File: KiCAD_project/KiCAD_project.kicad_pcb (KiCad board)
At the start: 2 copper layers, 3.6 x 3.3 mm, 17 parts, among them J1 Conn_01x04_Pin, SW1 SW_Push, SW10 RotaryEncoder_Switch, SW2 SW_Push, SW3 SW_Push, SW4 SW_Push, SW5 SW_Push, SW6 SW_Push, SW7 SW_Push, SW8 SW_Push, SW9 SW_Push, U1 XIAO-RP2040-DIP

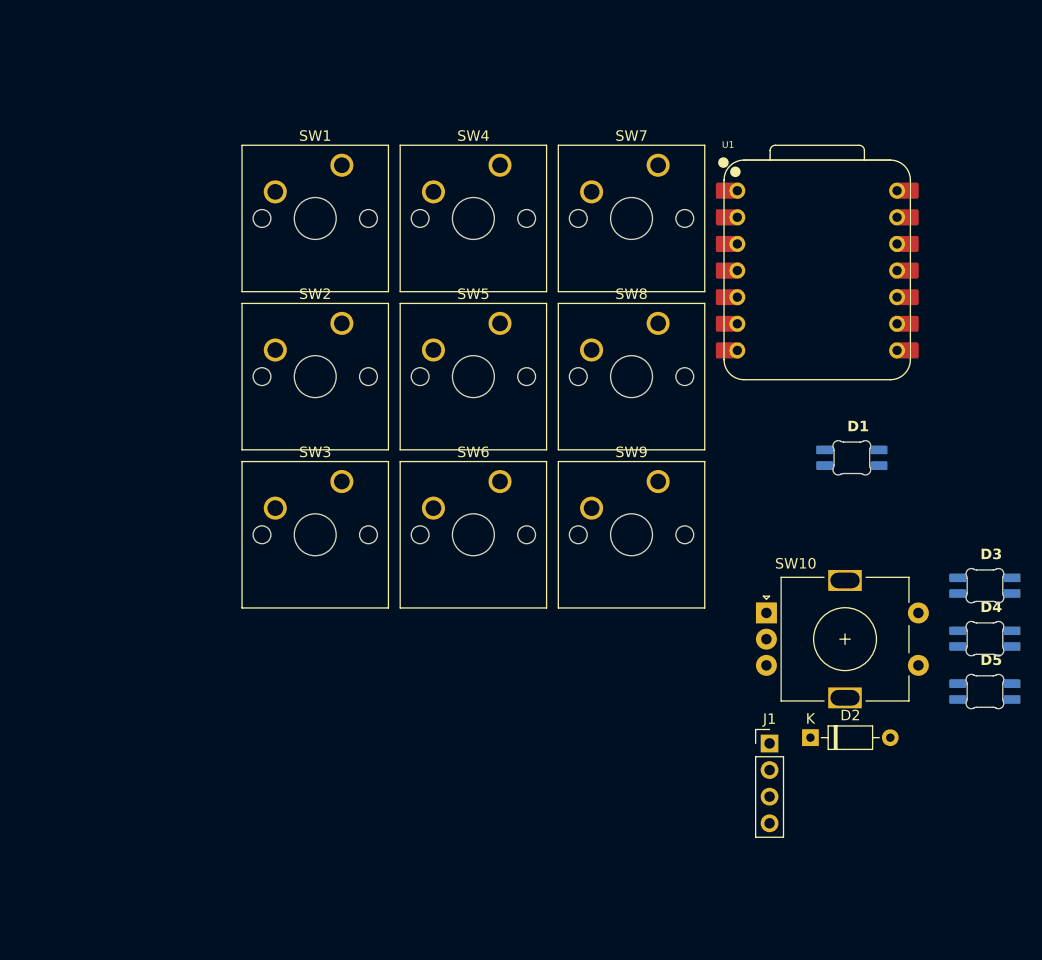
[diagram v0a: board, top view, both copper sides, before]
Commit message: added images and BOM into readme.md
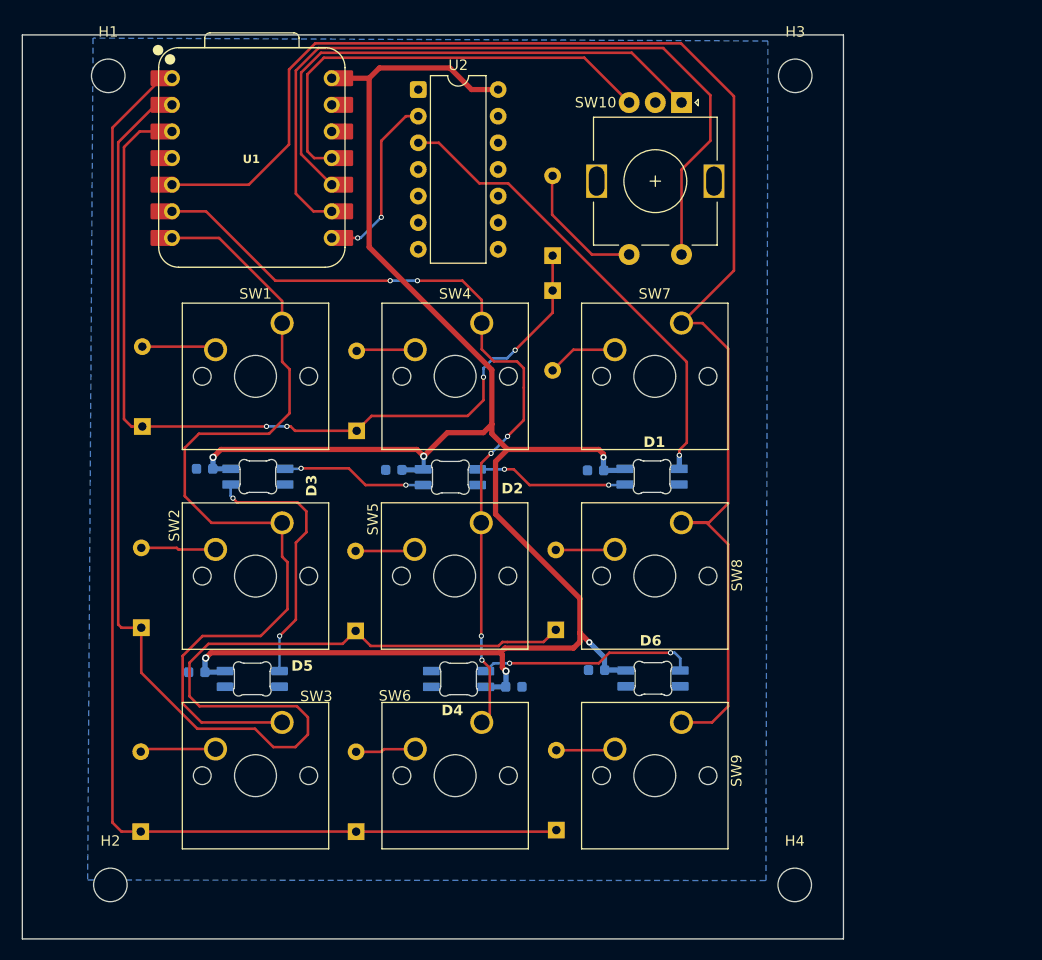
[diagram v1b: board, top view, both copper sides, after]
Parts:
- removed J1: Conn_01x04_Pin, Connector_PinHeader_2.54mm:PinHeader_1x04_P2.54mm_Vertical
- added C1: 100nF, Capacitor_SMD:C_0603_1608Metric, B.Cu at (151.2, 101.9)
- added C2: 100nF, Capacitor_SMD:C_0603_1608Metric, B.Cu at (131.9, 101.8)
- added C3: 100nF, Capacitor_SMD:C_0603_1608Metric, B.Cu at (113.8, 101.8)
- added C4: 100nF, Capacitor_SMD:C_0603_1608Metric, B.Cu at (113.1, 121.2)
- added C5: 100nF, Capacitor_SMD:C_0603_1608Metric, B.Cu at (143.3, 122.5)
- added C6: 100nF, Capacitor_SMD:C_0603_1608Metric, B.Cu at (151.2, 121.0)
- added D11: 1N4148, Diode_THT:D_DO-35_SOD27_P7.62mm_Horizontal, B.Cu at (107.9, 97.7)
- added D12: 1N4148, Diode_THT:D_DO-35_SOD27_P7.62mm_Horizontal, B.Cu at (107.8, 116.9)
- added D13: 1N4148, Diode_THT:D_DO-35_SOD27_P7.62mm_Horizontal, B.Cu at (128.3, 98.1)
- added D14: 1N4148, Diode_THT:D_DO-35_SOD27_P7.62mm_Horizontal, B.Cu at (128.2, 117.2)
- added D15: 1N4148, Diode_THT:D_DO-35_SOD27_P7.62mm_Horizontal, B.Cu at (147.1, 84.7)
- added D16: 1N4148, Diode_THT:D_DO-35_SOD27_P7.62mm_Horizontal, B.Cu at (147.3, 117.1)
- added D17: 1N4148, Diode_THT:D_DO-35_SOD27_P7.62mm_Horizontal, B.Cu at (107.8, 136.4)
- added D18: 1N4148, Diode_THT:D_DO-35_SOD27_P7.62mm_Horizontal, B.Cu at (128.3, 136.4)
- added D19: 1N4148, Diode_THT:D_DO-35_SOD27_P7.62mm_Horizontal, B.Cu at (147.4, 136.2)
- added D20: 1N4148, Diode_THT:D_DO-35_SOD27_P7.62mm_Horizontal, B.Cu at (147.1, 81.4)
- added D6: SK6812MINI-E, footprints:SK6812MINI-E_fixed, F.Cu at (156.6, 121.8)
- added H1: MountingHole, MountingHole:MountingHole_3.2mm_M3, F.Cu at (104.7, 64.2)
- added H2: MountingHole, MountingHole:MountingHole_3.2mm_M3, F.Cu at (104.8, 141.4)
- added H3: MountingHole, MountingHole:MountingHole_3.2mm_M3, F.Cu at (170.2, 64.2)
- added H4: MountingHole, MountingHole:MountingHole_3.2mm_M3, F.Cu at (170.2, 141.4)
- added U2: 74AHCT125, Package_DIP:DIP-14_W7.62mm, F.Cu at (134.2, 65.6)
- D2: value 1N4148 -> SK6812MINI-E; footprint Diode_THT:D_DO-35_SOD27_P7.62mm_Horizontal -> footprints:SK6812MINI-E_fixed
- moved D3 70.1 mm to (118.9, 102.6)
- moved D5 69.9 mm to (118.4, 121.9)
- moved U1 55.0 mm to (118.3, 72.1)
- moved D4 50.4 mm to (138.1, 121.7), turned to 180 degrees
- moved SW10 49.4 mm to (159.3, 66.8), turned to -90 degrees
- moved D2 42.4 mm to (137.3, 102.6)
- moved SW3 23.7 mm to (121.2, 125.9)
- moved SW9 23.1 mm to (159.3, 125.9)
- moved SW6 23.1 mm to (140.3, 125.9)
- moved SW2 19.9 mm to (121.2, 106.9)
- moved SW8 19.2 mm to (159.3, 106.9)
- moved D1 19.1 mm to (156.5, 102.6)
- moved SW5 19.1 mm to (140.2, 106.9)
- moved SW1 16.1 mm to (121.2, 87.8)
- moved SW7 15.2 mm to (159.3, 87.8)
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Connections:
- D1 pad 1: unconnected-(D1-VDD-Pad1) -> VBUS
- D1 pad 2: unconnected-(D1-DOUT-Pad2) -> Net-(D1-DOUT)
- D1 pad 3: unconnected-(D1-VSS-Pad3) -> GND
- D1 pad 4: unconnected-(D1-DIN-Pad4) -> Net-(D1-DIN)
- D2 pad 1: unconnected-(D2-K-Pad1) -> VBUS
- D2 pad 2: unconnected-(D2-A-Pad2) -> Net-(D2-DOUT)
- D3 pad 1: unconnected-(D3-VDD-Pad1) -> VBUS
- D3 pad 2: unconnected-(D3-DOUT-Pad2) -> Net-(D3-DOUT)
- D3 pad 3: unconnected-(D3-VSS-Pad3) -> GND
- D3 pad 4: unconnected-(D3-DIN-Pad4) -> Net-(D2-DOUT)
- D4 pad 1: unconnected-(D4-VDD-Pad1) -> VBUS
- D4 pad 2: unconnected-(D4-DOUT-Pad2) -> Net-(D4-DOUT)
- D4 pad 3: unconnected-(D4-VSS-Pad3) -> GND
- D4 pad 4: unconnected-(D4-DIN-Pad4) -> Net-(D4-DIN)
- D5 pad 1: unconnected-(D5-VDD-Pad1) -> VBUS
- D5 pad 2: unconnected-(D5-DOUT-Pad2) -> Net-(D4-DIN)
- D5 pad 3: unconnected-(D5-VSS-Pad3) -> GND
- D5 pad 4: unconnected-(D5-DIN-Pad4) -> Net-(D3-DOUT)
- SW1 pad 1: unconnected-(SW1-Pad1) -> COL1
- SW1 pad 2: unconnected-(SW1-Pad2) -> Net-(D11-A)
- SW10 pad A: unconnected-(SW10-PadA) -> Net-(U1-GPIO4/MISO)
- SW10 pad B: unconnected-(SW10-PadB) -> Net-(U1-GPIO3/MOSI)
- SW10 pad C: unconnected-(SW10-PadC) -> GND
- SW10 pad S1: unconnected-(SW10-PadS1) -> Net-(D20-A)
- SW10 pad S2: unconnected-(SW10-PadS2) -> COL4
- SW2 pad 1: unconnected-(SW2-Pad1) -> COL1
- SW2 pad 2: unconnected-(SW2-Pad2) -> Net-(D12-A)
- SW3 pad 1: unconnected-(SW3-Pad1) -> COL1
- SW3 pad 2: unconnected-(SW3-Pad2) -> Net-(D17-A)
- SW4 pad 1: unconnected-(SW4-Pad1) -> COL2
- SW4 pad 2: unconnected-(SW4-Pad2) -> Net-(D13-A)
- SW5 pad 1: unconnected-(SW5-Pad1) -> COL2
- SW5 pad 2: unconnected-(SW5-Pad2) -> Net-(D14-A)
- SW6 pad 1: unconnected-(SW6-Pad1) -> COL2
- SW6 pad 2: unconnected-(SW6-Pad2) -> Net-(D18-A)
- SW7 pad 1: unconnected-(SW7-Pad1) -> COL3
- SW7 pad 2: unconnected-(SW7-Pad2) -> Net-(D15-A)
- SW8 pad 1: unconnected-(SW8-Pad1) -> COL3
- SW8 pad 2: unconnected-(SW8-Pad2) -> Net-(D16-A)
- SW9 pad 1: unconnected-(SW9-Pad1) -> COL3
- SW9 pad 2: unconnected-(SW9-Pad2) -> Net-(D19-A)
- U1 pad 1: unconnected-(U1-GPIO26/ADC0/A0-Pad1) -> ROW3
- U1 pad 10: unconnected-(U1-GPIO4/MISO-Pad10) -> Net-(U1-GPIO4/MISO)
- U1 pad 11: unconnected-(U1-GPIO3/MOSI-Pad11) -> Net-(U1-GPIO3/MOSI)
- U1 pad 13: unconnected-(U1-GND-Pad13) -> GND
- U1 pad 14: unconnected-(U1-VBUS-Pad14) -> VBUS
- U1 pad 2: unconnected-(U1-GPIO27/ADC1/A1-Pad2) -> ROW2
- U1 pad 3: unconnected-(U1-GPIO28/ADC2/A2-Pad3) -> ROW1
- U1 pad 5: unconnected-(U1-GPIO6/SDA-Pad5) -> COL3
- U1 pad 6: unconnected-(U1-GPIO7/SCL-Pad6) -> COL2
- U1 pad 7: unconnected-(U1-GPIO0/TX-Pad7) -> COL1
- U1 pad 8: unconnected-(U1-GPIO1/RX-Pad8) -> Net-(U1-GPIO1/RX)
- U1 pad 9: unconnected-(U1-GPIO2/SCK-Pad9) -> COL4
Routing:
- net VBUS: track 0.00 -> 179.7 mm, vias 0 -> 6
- net COL3: track 0.00 -> 140.5 mm
- net ROW2: track 0.00 -> 133.0 mm
- net ROW3: track 0.00 -> 116.9 mm
- net COL1: track 0.00 -> 86.2 mm
- net ROW1: track 0.00 -> 84.5 mm, vias 0 -> 4
- net COL2: track 0.00 -> 78.7 mm, vias 0 -> 6
- net COL4: track 0.00 -> 74.5 mm
- net Net-(U1-GPIO4/MISO): track 0.00 -> 51.0 mm
- net Net-(D1-DIN): track 0.00 -> 44.8 mm, vias 0 -> 1
- net Net-(U1-GPIO3/MOSI): track 0.00 -> 43.9 mm
- net Net-(D3-DOUT): track 0.00 -> 25.2 mm, vias 0 -> 2
- net Net-(D4-DOUT): track 0.00 -> 20.7 mm, vias 0 -> 2
- net Net-(U1-GPIO1/RX): track 0.00 -> 18.2 mm, vias 0 -> 2
- net Net-(D1-DOUT): track 0.00 -> 14.7 mm, vias 0 -> 2
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- added copper zone on B.Cu, net GND
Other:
- board size 3.6 x 3.3 mm -> 78.4 x 86.2 mm

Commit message: Added edited PCB and CAD
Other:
- board text added: "saman_0"
